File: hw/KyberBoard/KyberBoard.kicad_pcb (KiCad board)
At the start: 4 copper layers, 60.7 x 27.2 mm, 73 parts, among them J1 282834-2, J2 282834-2, J3 OSTVN12A150, J4 NUCLEO144ZE-STLINK, Q1 STL120N4F6AG, Q2 SIS413DN-T1-GE3, Q3 SSM3K337R, Q4 STL76DN4LF7AG, Q5 SSM3K337R, Q6 SSM3K337R, Q7 SSM3K337R, SW1 SW, U1 STM32L051K8Tx, U2 VNHD7008AY, U3 AZ1117IH-3.3TRG1, U4 MMA8452Q

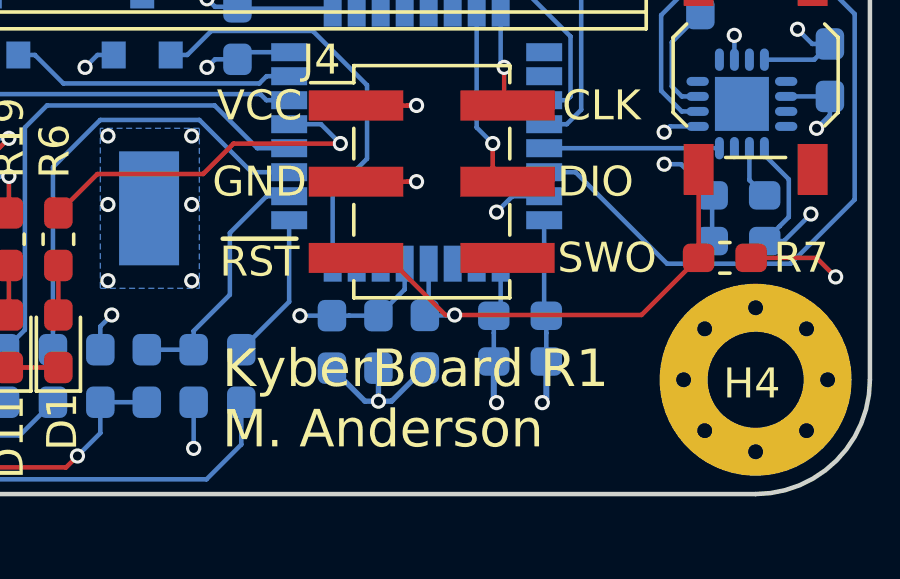
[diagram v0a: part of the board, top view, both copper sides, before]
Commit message: renamed PCB project to KyberBoard
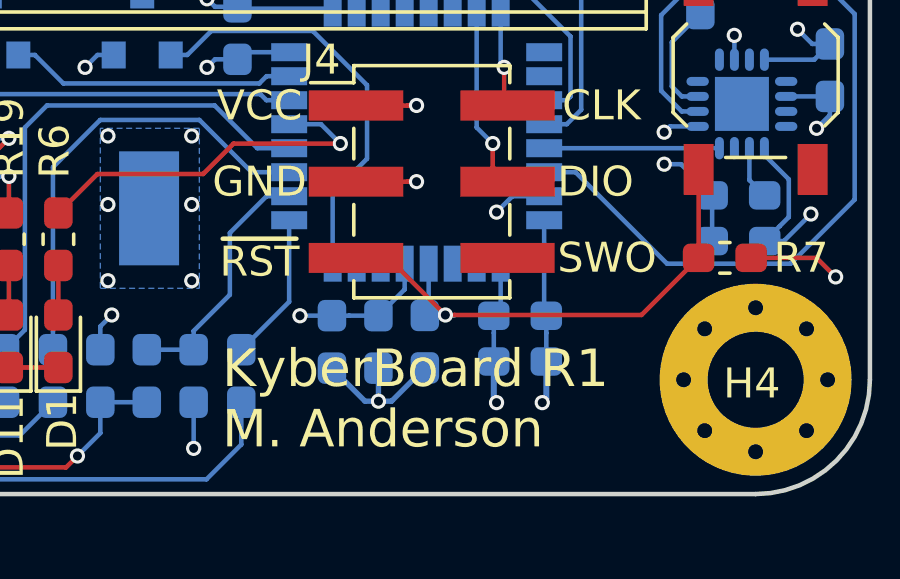
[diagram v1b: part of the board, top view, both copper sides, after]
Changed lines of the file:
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@@
   (layers
     (0 F.Cu signal)
-    (1 In1.Cu power)
+    (1 In1.Cu power hide)
     (2 In2.Cu power hide)
-    (31 B.Cu signal)
+    (31 B.Cu signal hide)
     (32 B.Adhes user hide)
     (33 F.Adhes user hide)
@@
     (44 Edge.Cuts user)
     (45 Margin user hide)
-    (46 B.CrtYd user)
+    (46 B.CrtYd user hide)
     (47 F.CrtYd user hide)
     (48 B.Fab user hide)
@@
   )
   (setup
-    (last_trace_width 0.381)
+    (last_trace_width 0.2)
     (user_trace_width 0.1524)
     (user_trace_width 0.1778)
@@
   (segment (start 162.329151 82.744956) (end 162.329151 84.342) (width 0.1524) (layer B.Cu) (net 60))
   (segment (start 162.202151 84.469) (end 162.447 84.469) (width 0.1524) (layer B.Cu) (net 60))
-  (via (at 163.195 84.455) (size 0.508) (drill 0.29972) (layers F.Cu B.Cu) (net 60))
+  (via (at 162.885886 84.455) (size 0.508) (drill 0.29972) (layers F.Cu B.Cu) (net 60))
   (segment (start 162.202151 84.469) (end 163.181 84.469) (width 0.1524) (layer B.Cu) (net 60))
   (segment (start 163.181 84.469) (end 163.195 84.455) (width 0.1524) (layer B.Cu) (net 60))
@@
     (polygon
       (pts
-        (xy 177.8 62.992) (xy 177.8 91.44) (xy 114.427 91.392) (xy 114.427 87.328) (xy 138.176 87.328)
+        (xy 177.8 62.992) (xy 177.8 91.44) (xy 115.57 91.39248) (xy 115.57 87.32752) (xy 138.176 87.328)
         (xy 138.176 81.74) (xy 143.891 81.74) (xy 143.891 62.992)
       )
@@
     (polygon
       (pts
-        (xy 138.1125 62.992) (xy 114.427 62.992) (xy 114.427 87.328) (xy 138.1125 87.63)
+        (xy 138.1125 62.992) (xy 115.57 63.001015) (xy 115.57 87.318985) (xy 138.1125 87.63)
       )
     )

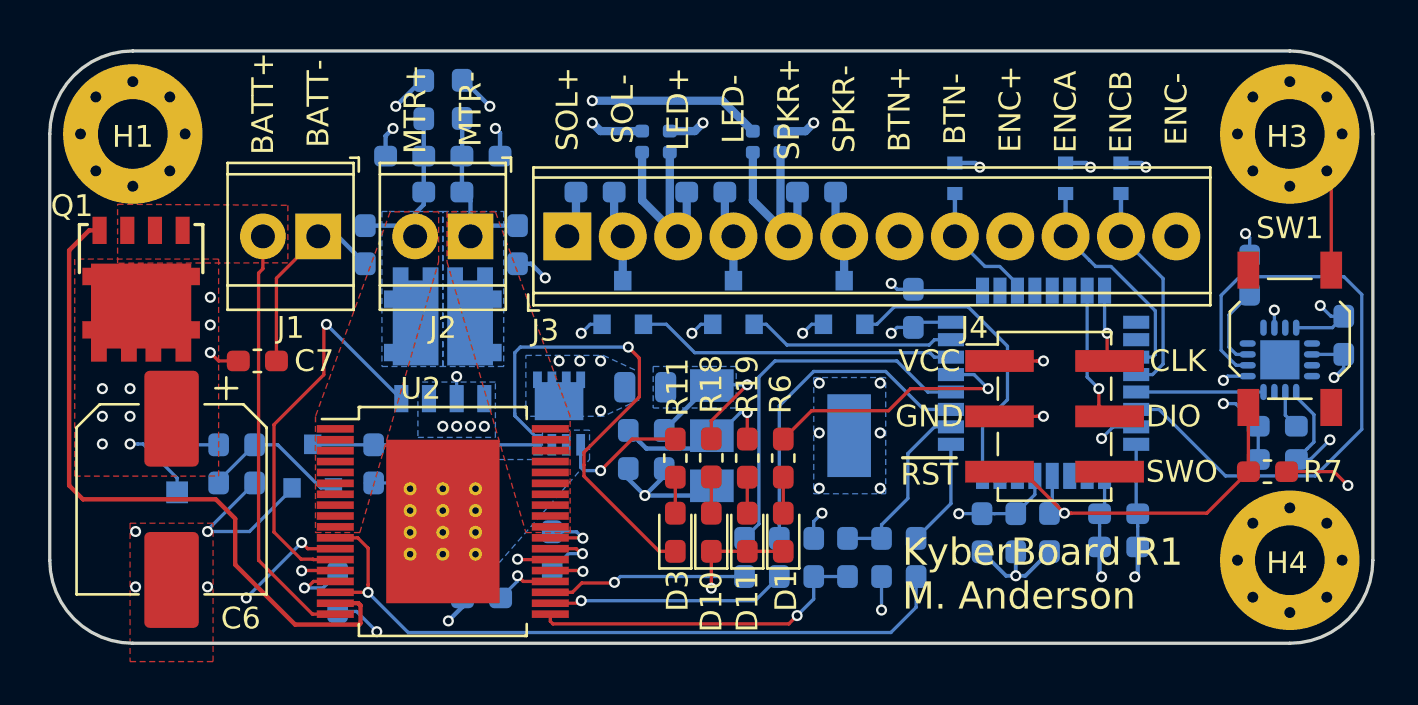
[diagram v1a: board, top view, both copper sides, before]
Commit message: working adc code and minor circuit correction
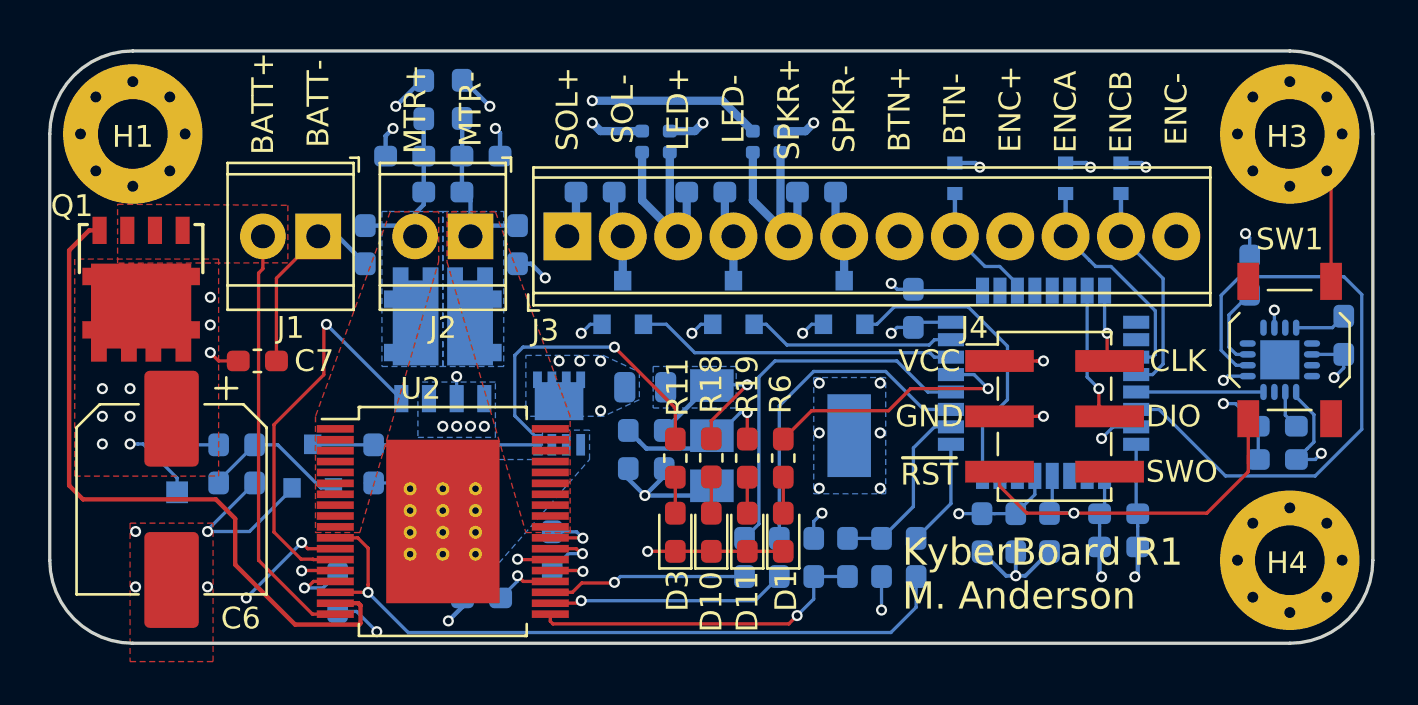
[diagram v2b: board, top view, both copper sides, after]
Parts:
- removed R7: 1k, Resistor_SMD:R_0603_1608Metric_Pad1.05x0.95mm_HandSolder
- D13, D14, D15: value BZT585B4V3T-7 -> BZT585B3V6T
- R11: value 1K -> 0
- moved SW1 0.52 mm to (173.2, 77.0)
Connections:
- D3 pad 1: Net-(D3-Pad1) -> GND
- Q2 pad 4: Net-(D3-Pad1) -> Net-(Q2-Pad4)
- Q3 pad 3: Net-(D3-Pad1) -> Net-(Q2-Pad4)
- R11 pad 1: /hbridge/VCC -> Net-(Q2-Pad4)
- R8 pad 2: Net-(D3-Pad1) -> Net-(Q2-Pad4)
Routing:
- net Net-(D3-Pad1): track 33.5 -> 0.00 mm, vias 1 -> 0
- net Net-(Q2-Pad4): track 0.00 -> 25.3 mm, vias 0 -> 1
- net /hbridge/VCC: track 15.1 -> 9.06 mm, vias 12 -> 11
- net +3V3: track 44.5 -> 40.8 mm, vias 18 -> 17
- net GND: track 107.8 -> 111.0 mm, vias 36 -> 35
- net /micro/NRST: track 19.7 -> 21.1 mm

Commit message: prepping board for fab -- DRC,easter eggs,silkscreen
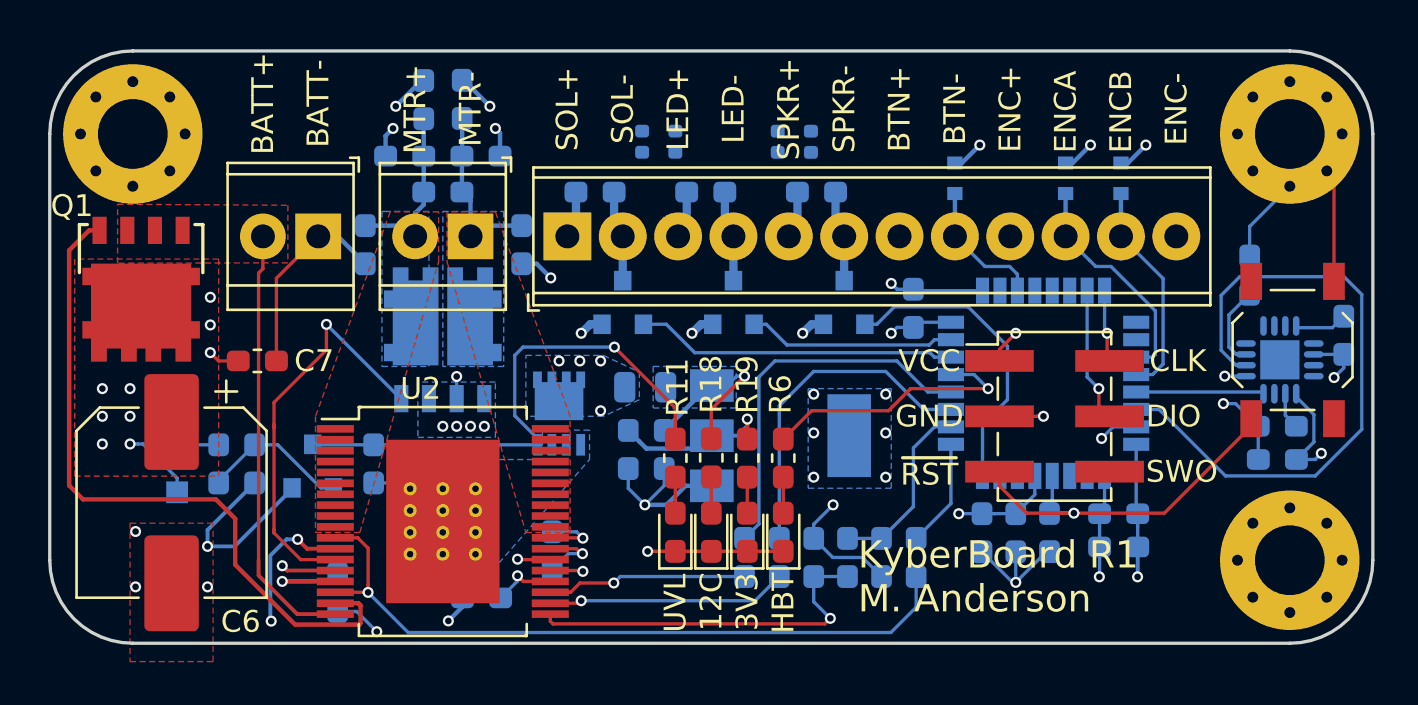
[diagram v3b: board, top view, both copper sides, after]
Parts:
- removed D3: 150060RS75020, LED_SMD:LED_0603_1608Metric_Pad1.05x0.95mm_HandSolder
- removed R14, R15: 0, Resistor_SMD:R_0402_1005Metric
- removed SW1: SW, Button_Switch_SMD:SW_SPST_TL3342
- added 12V: 0, Resistor_SMD:R_0402_1005Metric, B.Cu at (143.5, 67.4)
- added 3V3: 0, Resistor_SMD:R_0402_1005Metric, B.Cu at (145.0, 67.4)
- added ?: SW, Button_Switch_SMD:SW_SPST_TL3342, F.Cu at (173.4, 77.0)
- added G***: LOGO, easter-eggs:starfleet, B.Cu at (162.1, 78.7)
- added G***: LOGO, easter-eggs:qr-funeral-pyre, B.Cu at (120.0, 74.3)
- added UVL: 150060RS75020, LED_SMD:LED_0603_1608Metric_Pad1.05x0.95mm_HandSolder, F.Cu at (145.0, 85.3)
- U4: footprint Package_DFN_QFN:QFN-16-1EP_3x3mm_P0.5mm_EP1.8x1.8mm -> MMA8542:QFN-16-1EP_3x3mm_P0.5mm_EP1.8x1.8mm
- moved 3V3 1.40 mm to (151.3, 67.4)
- moved 12V 1.14 mm to (149.7, 67.4)
- moved C11 0.19 mm to (138.0, 72.1)
- moved C6 0.15 mm to (121.9, 84.0)
- renumbered D10 to 12C, R16 to 12V, R17 to 3V3, D11 to 3V3, J3 to ?, H1 to ?, H3 to ?, H4 to ?, J1 to ?, J2 to ?, J4 to ?, D1 to HBT
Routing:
- net GND: track 111.0 -> 124.4 mm, vias 35 -> 32
- net +12V: track 12.6 -> 2.20 mm, vias 6 -> 4
- net /LED+: track 13.5 -> 5.47 mm
- net /SPKR+: track 12.4 -> 4.35 mm
- net +3V3: track 40.8 -> 38.2 mm, vias 17 -> 15
- net Net-(R12-Pad1): track 3.34 -> 5.13 mm
- net /hbridge/imtr: track 15.5 -> 17.1 mm
- net /micro/NRST: track 21.1 -> 20.0 mm
- net /BTN: track 6.04 -> 6.61 mm
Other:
- net class Default: clearance 0.2032 -> 0.13
- rule trace_clearance: 0.2032 -> 0.13

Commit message: corrected FET footprint (missing mask on pad) and more easter eggs
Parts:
- added G***: LOGO, easter-eggs:velociraptor, F.Cu at (171.2, 73.2)
- added G***: LOGO, easter-eggs:tatooine-travel-poster, B.Cu at (126.5, 76.7)
- moved G*** 9.58 mm to (126.0, 66.8)

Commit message: cleaned silkscreen and checked design rules. almost ready for fab
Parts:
- removed 12V (x2): 0, Resistor_SMD:R_0402_1005Metric
- removed the 3V3 at (145.0, 67.4)
- removed the G*** at (126.5, 76.7)
- added 12: 0, Resistor_SMD:R_0402_1005Metric, B.Cu at (150.0, 67.8)
- added 12: 0, Resistor_SMD:R_0402_1005Metric, B.Cu at (145.0, 67.8)
- added 3.3: 0, Resistor_SMD:R_0402_1005Metric, B.Cu at (146.1, 67.8)
- added G***: LOGO, easter-eggs:jediorder, B.Cu at (129.4, 85.9)
- added G***: LOGO, easter-eggs:saber, B.Cu at (170.8, 89.5)
- moved G*** 9.48 mm to (120.0, 74.2)
- moved 3.3 0.42 mm to (151.1, 67.8)
- moved D4 0.14 mm to (132.7, 68.2)
- moved D5 0.14 mm to (136.2, 68.2)
- moved D6 0.10 mm to (133.6, 65.4)
- moved C9 0.09 mm to (134.4, 69.8)
- moved D7 0.08 mm to (135.3, 65.4)
- renumbered 3V3 to 3.3
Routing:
- net +12V: track 2.20 -> 13.4 mm, vias 4 -> 6
- net +3V3: track 38.2 -> 42.2 mm, vias 15 -> 17
- net /SPKR+: track 4.35 -> 7.66 mm
- net /LED+: track 5.47 -> 8.78 mm
- net /hbridge/VCC: track 9.06 -> 9.87 mm
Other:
- board text added: "By the right of the Council, by the will of the Force..."
- board text added: "LED"
- board text added: "SPKR"

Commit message: board ready to send out to fab
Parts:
- added G***: LOGO, easter-eggs:clankryze, B.Cu at (157.5, 85.6)
- moved G*** 0.18 mm to (129.5, 86.0)
- moved G*** 0.13 mm to (120.0, 74.3)
- moved 12 0.06 mm to (150.1, 67.8)
- moved 3.3 0.06 mm to (151.2, 67.8)
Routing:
- net GND: track 124.4 -> 127.2 mm, vias 32 -> 34
- net +3V3: track 42.2 -> 41.1 mm

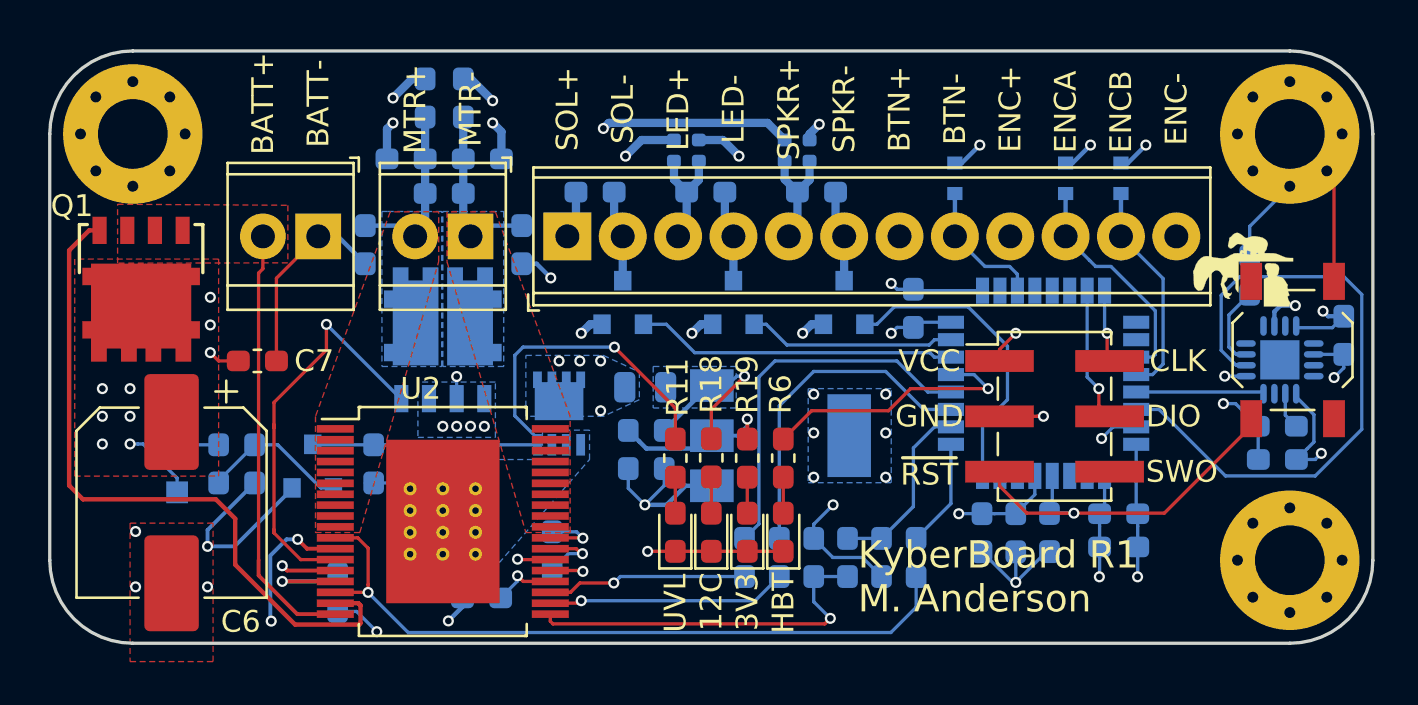
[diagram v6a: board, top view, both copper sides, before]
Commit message: found major ACC footprint error. Corrected + redid local placement + routing
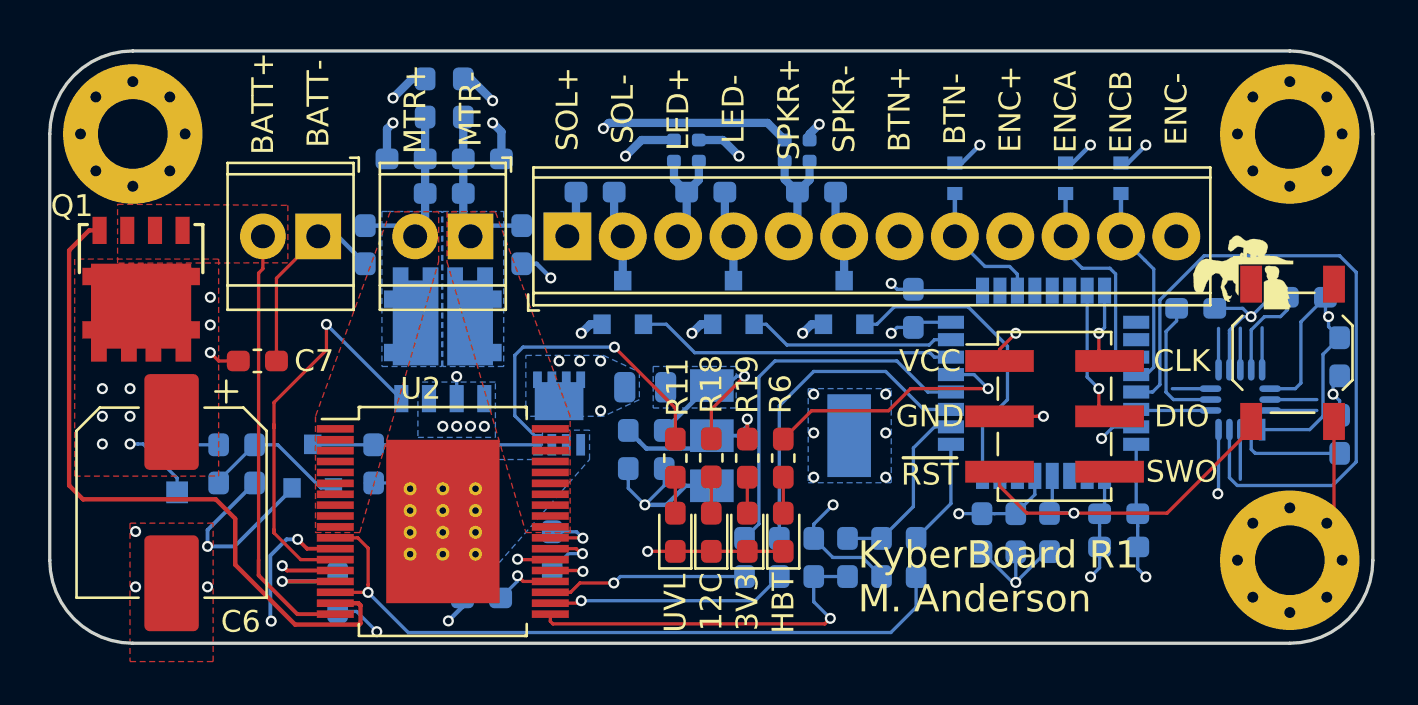
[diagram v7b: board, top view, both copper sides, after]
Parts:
- U4: footprint MMA8542:QFN-16-1EP_3x3mm_P0.5mm_EP1.8x1.8mm -> MMA8542:MMA8452Q
- moved C15 5.51 mm to (175.5, 77.3), turned to 90 degrees
- moved R20 2.91 mm to (168.9, 75.1), turned to 0 degrees
- moved C17 2.88 mm to (175.5, 80.8), turned to 270 degrees
- moved U4 2.59 mm to (170.9, 79.2)
- moved C16 2.45 mm to (174.0, 74.5), turned to 0 degrees
- moved ? 0.13 mm to (173.4, 77.1)
- moved G*** 0.13 mm to (171.2, 73.3)
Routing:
- net /acc/SCL: track 5.85 -> 32.6 mm
- net /acc/SDA: track 29.9 -> 3.52 mm
- net (no net): track 0.00 -> 10.6 mm
- net +3V3: track 41.1 -> 49.2 mm, vias 17 -> 16
- net GND: track 127.2 -> 132.6 mm, vias 34 -> 33
- net Net-(C17-Pad2): track 1.78 -> 5.14 mm
- net Net-(R20-Pad1): track 3.82 -> 6.32 mm
- net Net-(U4-Pad11): track 0.00 -> 2.01 mm
- net Net-(U4-Pad9): track 0.00 -> 1.99 mm
- net /ENC_B: track 11.1 -> 10.6 mm
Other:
- rule pad_to_mask_clearance: 0.051 -> 0.05
- rule solder_mask_min_width: 0.25 -> 0.2
